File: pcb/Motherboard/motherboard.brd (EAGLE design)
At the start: 50.8 x 49.5 mm, 22 parts, among them U1 MIC5219 3.3V

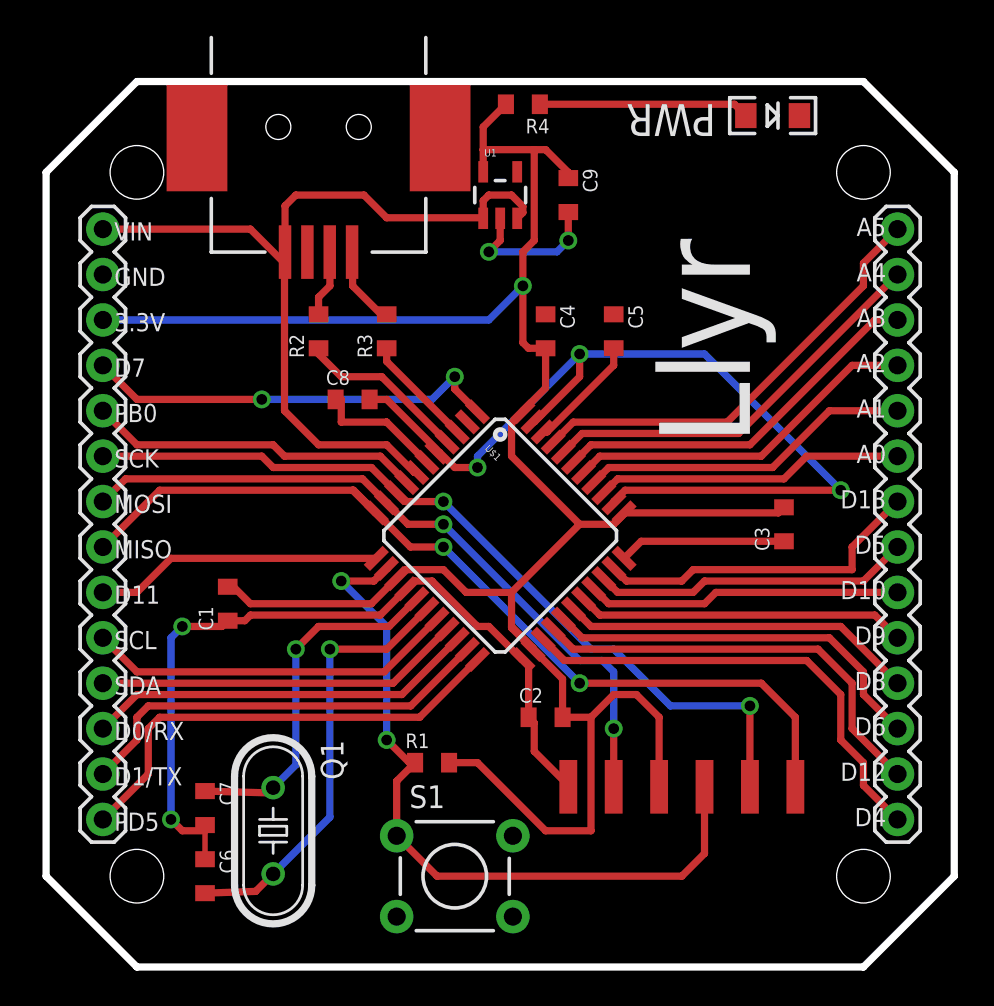
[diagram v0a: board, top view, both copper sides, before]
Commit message: Added sensor board and reorganized
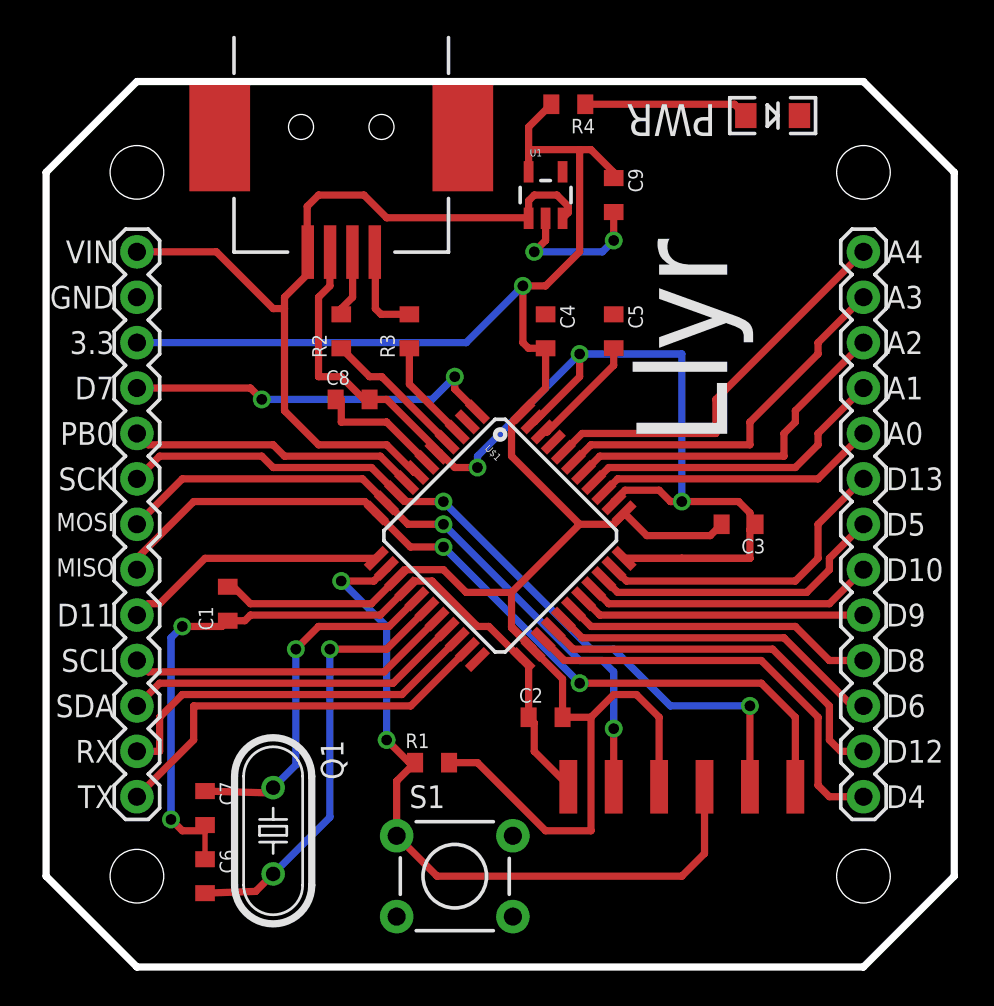
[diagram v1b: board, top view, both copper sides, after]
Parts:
- JP2, JP3: device SparkFun-Connectors:1X14 -> SparkFun-Connectors:1X13
- moved C3 2.54 mm to (66.7, 34.9), turned to 180 degrees
- moved C9 2.54 mm to (59.7, 53.3)
- moved R4 2.54 mm to (57.1, 58.4)
- moved U1 2.54 mm to (55.9, 53.3)
- moved JP2 2.29 mm to (33.0, 50.2)
- moved JP3 2.29 mm to (73.7, 50.2)
- moved JP1 1.27 mm to (44.5, 57.1)
- moved R2 1.27 mm to (44.5, 45.7)
- moved R3 1.27 mm to (48.3, 45.7)
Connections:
- removed net PD5: JP2.14, U$1.22
- net PB4: now also JP3.10; no longer JP3.11
- net PB5: now also JP3.9; no longer JP3.10
- net PB6: now also JP3.8; no longer JP3.9
- net PC6: now also JP3.7; no longer JP3.8
- net PC7: now also JP3.6; no longer JP3.7
- net PD4: now also JP3.13; no longer JP3.14
- net PD6: now also JP3.12; no longer JP3.13
- net PD7: now also JP3.11; no longer JP3.12
- net PF0: no longer JP3.1
- net PF1: now also JP3.1; no longer JP3.2
- net PF4: now also JP3.2; no longer JP3.3
- net PF5: now also JP3.3; no longer JP3.4
- net PF6: now also JP3.4; no longer JP3.5
- net PF7: now also JP3.5; no longer JP3.6
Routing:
- net PD5: track 26.1 -> 0.00 mm
- net PF0: track 24.9 -> 0.00 mm
- net GND: track 116.1 -> 124.8 mm
- net MISO: track 51.1 -> 47.7 mm
- net PD7: track 22.0 -> 18.8 mm
- net PD6: track 24.1 -> 21.3 mm
- net N$6: track 11.8 -> 9.24 mm
- net PB4: track 19.8 -> 17.4 mm
- net PE6: track 23.5 -> 21.1 mm
- net PD4: track 26.2 -> 23.8 mm
- net PD0: track 20.7 -> 18.3 mm
- net PB5: track 18.5 -> 16.0 mm
- net PB0: track 18.7 -> 16.2 mm
- net 3.3V: track 130.2 -> 127.8 mm
- net D+: track 9.55 -> 8.09 mm
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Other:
- board text added: "3.3"
- board text added: "C AberSailbot"
- board text added: "RX"
- board text added: "TX"
- board text removed: "A5"
- board text removed: "D0/RX"
- board text removed: "D1/TX"
- board text removed: "PD5"
